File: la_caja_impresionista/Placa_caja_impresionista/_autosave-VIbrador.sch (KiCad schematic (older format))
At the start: 15 parts, among them U3 Buzzer, U4 HC-05, U5 Buzzer, U6 PiZeroW

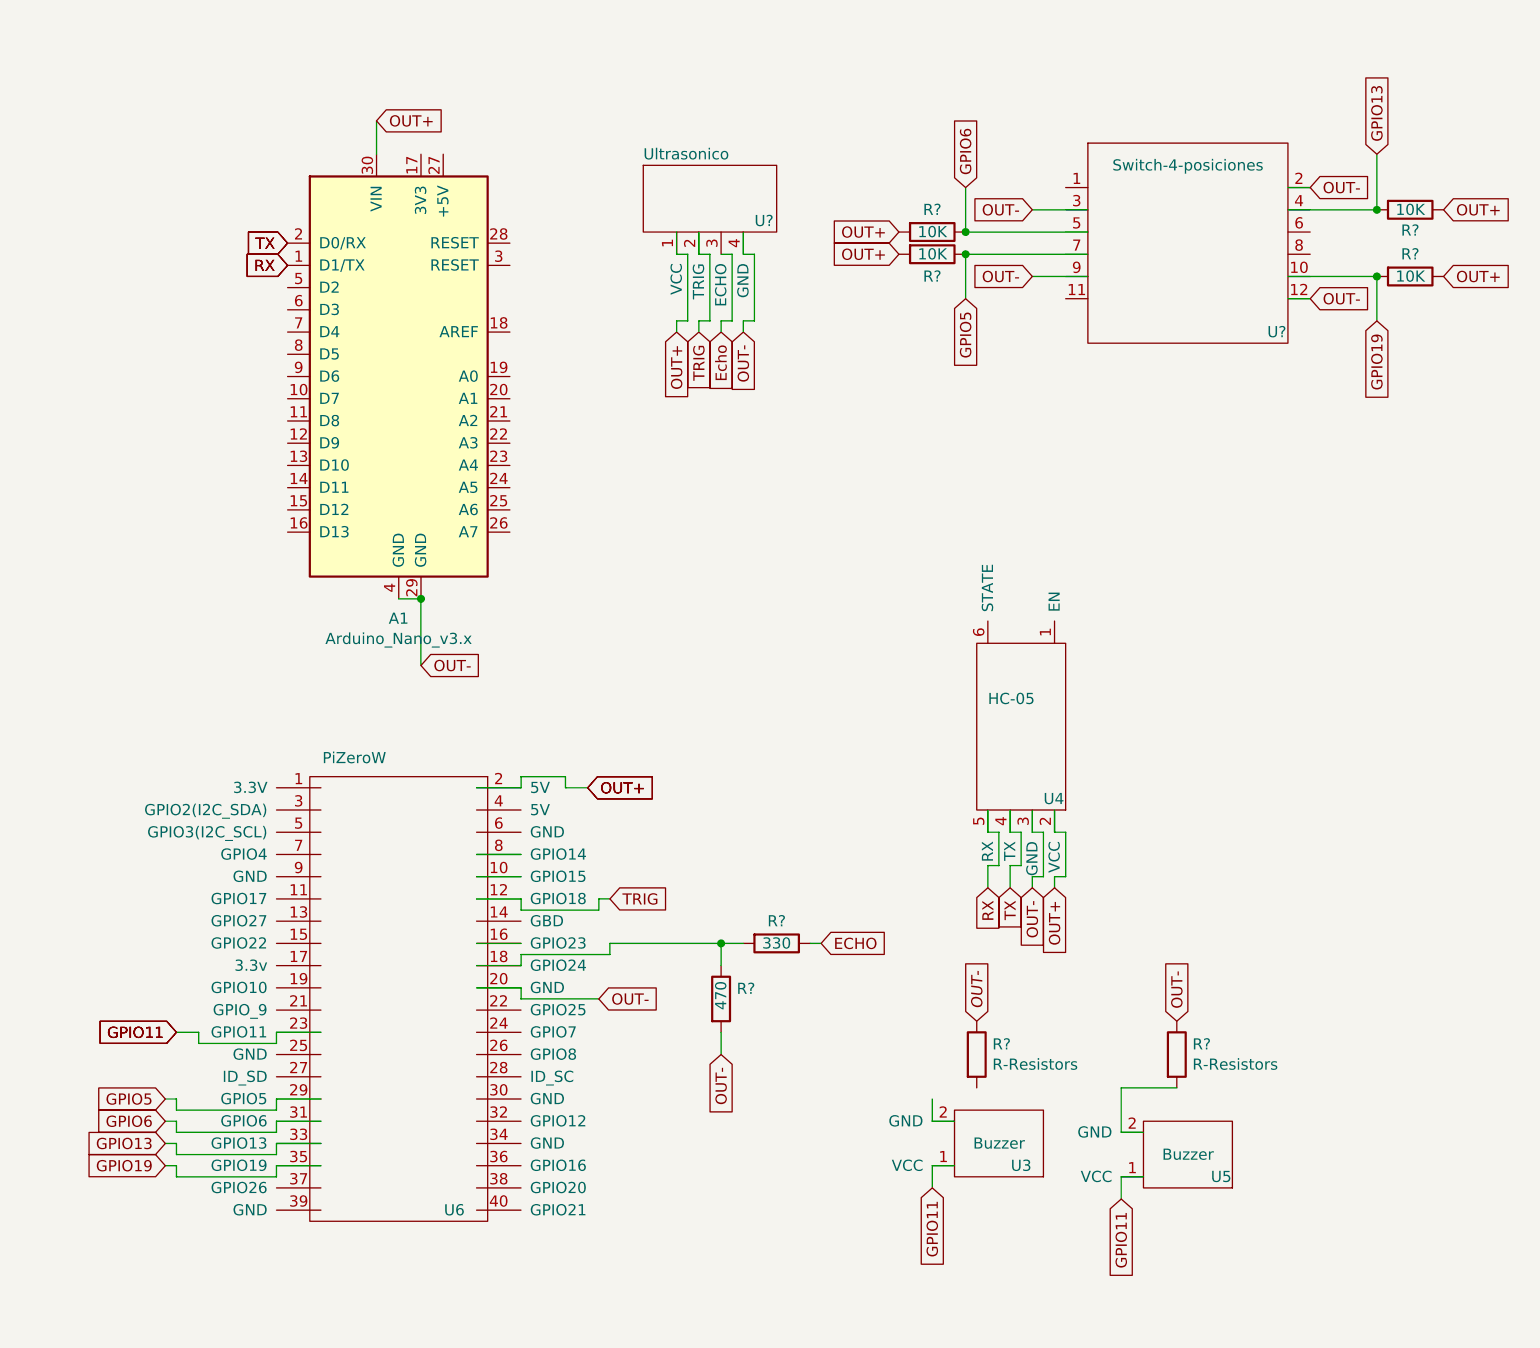
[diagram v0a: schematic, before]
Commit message: Conexiones PCB
Quedo conectado todo feo y como el orto pero esta conectado que es mejor que nada despues hay que revisar todas las conexiones y dejarlas facheras
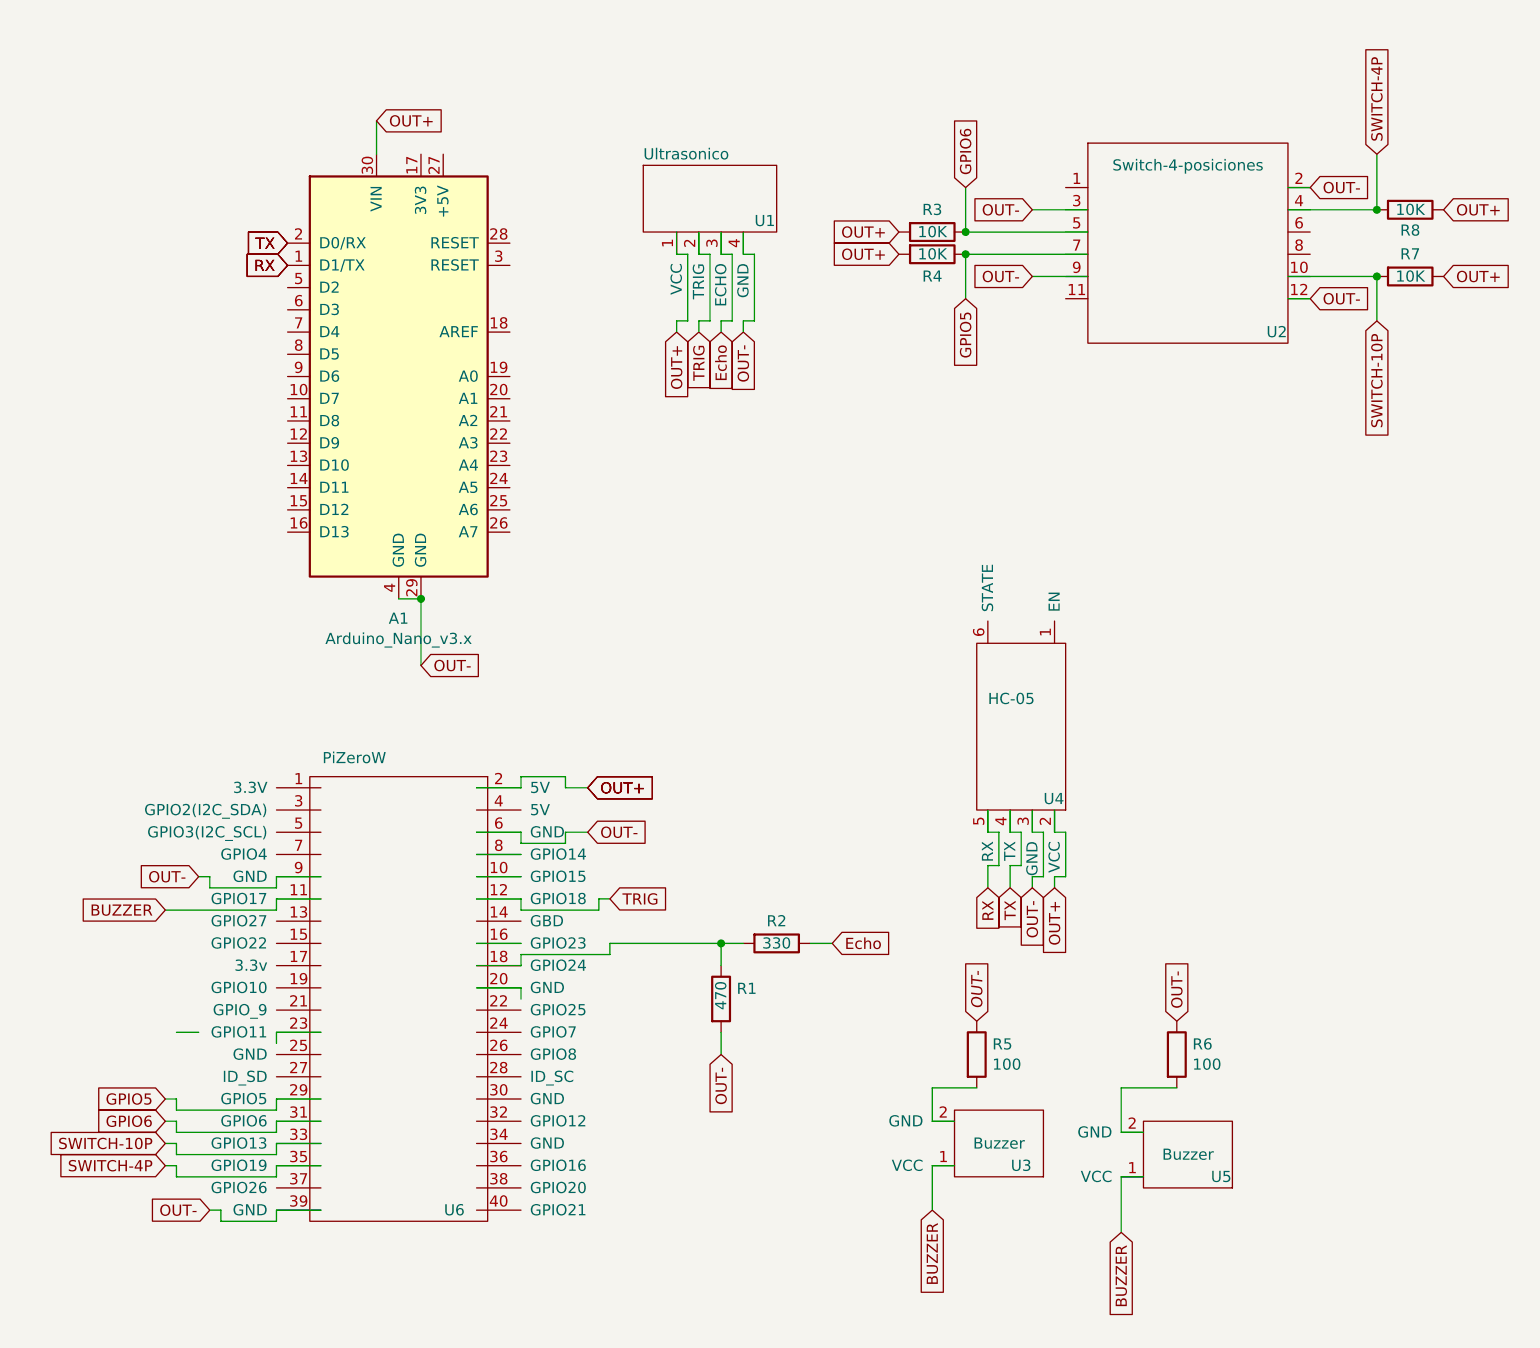
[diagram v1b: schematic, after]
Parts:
- A1: footprint Module:Arduino_Nano -> Raspberry:Arduino_Nano
- R1, R2, R3, R4, R7, R8: renamed from R?; footprint (none) -> devices:R_Axial_DIN0207_L6.3mm_D2.5mm_P10.16mm_Horizontal
- R5, R6: renamed from R?; value R-Resistors -> 100; footprint (none) -> devices:R_Axial_DIN0207_L6.3mm_D2.5mm_P10.16mm_Horizontal
- U1: renamed from U?; footprint (none) -> VibradorPCB:Ultrasonico
- U2: renamed from U?; footprint (none) -> VibradorPCB:Switch_4_posiciones
- U6: footprint Module:Raspberry_Pi_Zero_Socketed_THT_FaceDown_MountingHoles -> Raspberry:Raspberry_Pi_Zero_Socketed_THT_FaceDown_MountingHoles
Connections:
- net labels added: BUZZER, SWITCH-10P, SWITCH-4P
- net labels removed: ECHO, GPIO11, GPIO13, GPIO19
- wire segments 113 -> 130
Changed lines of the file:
@@
 Wire Wire Line
 	5350 6050 5250 6050
-Wire Wire Line
-	5250 6050 5250 6150
 Text GLabel 5450 5400 1    50   Input Italic 0
 OUT-
-Wire Wire Line
-	5250 5850 5250 5750
 Wire Wire Line
 	5250 5850 5350 5850
@@
 Wire Wire Line
 	6200 6100 6100 6100
-Wire Wire Line
-	6100 6100 6100 6200
 Text GLabel 6350 5400 1    50   Input ~ 0
 OUT-
@@
 $EndComp
 $Comp
-L VIbrador-rescue:PiZeroW U6
-U 1 1 5E9167F3
-P 2800 4300
-F 0 "U6" H 3100 2350 50  0000 C CNN
-F 1 "PiZeroW" H 2650 4384 50  0000 C CNN
-F 2 "Module:Raspberry_Pi_Zero_Socketed_THT_FaceDown_MountingHoles" H 2800 4300 50  0001 C CNN
-F 3 "" H 2800 4300 50  0001 C CNN
-	1    2800 4300
-	1    0    0    -1
-$EndComp
-$Comp
 L VIbrador-rescue:Arduino_Nano_v3.x-MCU_Module-VIbrador-rescue A1
 U 1 1 5E91EE2F
@@
 F 0 "A1" H 2850 1411 50  0000 C CNN
 F 1 "Arduino_Nano_v3.x" H 2850 1320 50  0000 C CNN
-F 2 "Module:Arduino_Nano" H 3000 1550 50  0001 L CNN
+F 2 "Raspberry:Arduino_Nano" H 3000 1550 50  0001 L CNN
 F 3 "http://www.mouser.com/pdfdocs/Gravitech_Arduino_Nano3_0.pdf" H 2850 1500 50  0001 C CNN
 	1    2850 2500
@@
 Wire Wire Line
 	3400 4350 3200 4350
-Text GLabel 3750 5300 2    50   Input ~ 0
+Text GLabel 3700 4550 2    50   Input ~ 0
 OUT-
 Wire Wire Line
@@
 Wire Wire Line
 	3400 5150 3200 5150
-Text GLabel 5250 6150 3    50   Input ~ 0
-GPIO11
-Text GLabel 6100 6200 3    50   Input ~ 0
-GPIO11
-Text GLabel 1850 5450 0    50   Input ~ 0
-GPIO11
 Wire Wire Line
 	2500 5450 2300 5450
 Wire Wire Line
 	2300 5450 2300 5500
-Wire Wire Line
-	2300 5500 1950 5500
-Wire Wire Line
-	1950 5500 1950 5450
 Wire Wire Line
 	1950 5450 1850 5450
@@
 RX
 $Comp
-L VIbrador-rescue:Ultrasonico-VIbrador-rescue U?
+L VIbrador-rescue:Ultrasonico-VIbrador-rescue U1
 U 1 1 5F11CF15
 P 4250 1600
-F 0 "U?" H 4450 1400 50  0000 L CNN
+F 0 "U1" H 4450 1400 50  0000 L CNN
 F 1 "Ultrasonico" H 3950 1700 50  0000 L CNN
-F 2 "" H 4250 1600 50  0001 C CNN
+F 2 "VibradorPCB:Ultrasonico" H 4250 1600 50  0001 C CNN
 F 3 "" H 4250 1600 50  0001 C CNN
 	1    4250 1600
@@
 Text GLabel 3700 4350 2    50   Input ~ 0
 OUT+
-Text GLabel 4750 5050 2    50   Input ~ 0
-ECHO
-Wire Wire Line
-	3400 5300 3750 5300
 Wire Wire Line
 	3400 5150 3400 5100
@@
 	3800 5100 3800 5050
 $Comp
-L VIbrador-rescue:R-Resistors R?
+L VIbrador-rescue:R-Resistors R1
 U 1 1 5F12F5BA
 P 4300 5300
-F 0 "R?" H 4370 5346 50  0000 L CNN
+F 0 "R1" H 4370 5346 50  0000 L CNN
 F 1 "470" V 4300 5250 50  0000 L CNN
-F 2 "" V 4230 5300 50  0001 C CNN
+F 2 "devices:R_Axial_DIN0207_L6.3mm_D2.5mm_P10.16mm_Horizontal" V 4230 5300 50  0001 C CNN
 F 3 "~" H 4300 5300 50  0001 C CNN
 	1    4300 5300
@@
 $EndComp
 $Comp
-L VIbrador-rescue:R-Resistors R?
+L VIbrador-rescue:R-Resistors R2
 U 1 1 5F12598C
 P 4550 5050
-F 0 "R?" V 4450 5050 50  0000 C CNN
+F 0 "R2" V 4450 5050 50  0000 C CNN
 F 1 "330" V 4550 5050 50  0000 C CNN
-F 2 "" V 4480 5050 50  0001 C CNN
+F 2 "devices:R_Axial_DIN0207_L6.3mm_D2.5mm_P10.16mm_Horizontal" V 4480 5050 50  0001 C CNN
 F 3 "~" H 4550 5050 50  0001 C CNN
 	1    4550 5050
@@
 $EndComp
 Wire Wire Line
-	4750 5050 4700 5050
-Wire Wire Line
 	3800 5050 4300 5050
 Wire Wire Line
@@
 	4300 5450 4300 5550
 $Comp
-L VIbrador-rescue:Switch-4-posiciones-VIbrador-rescue U?
+L VIbrador-rescue:Switch-4-posiciones-VIbrador-rescue U2
 U 1 1 5F14136B
 P 6450 1650
-F 0 "U?" H 6800 1000 50  0000 C CNN
+F 0 "U2" H 6800 1000 50  0000 C CNN
 F 1 "Switch-4-posiciones" H 6400 1750 50  0000 C CNN
-F 2 "" H 6450 1650 50  0001 C CNN
+F 2 "VibradorPCB:Switch_4_posiciones" H 6450 1650 50  0001 C CNN
 F 3 "" H 6450 1650 50  0001 C CNN
 	1    6450 1650
@@
 	5950 2050 5700 2050
 $Comp
-L VIbrador-rescue:R-Resistors R?
+L VIbrador-rescue:R-Resistors R7
 U 1 1 5F14B51D
 P 7400 1750
-F 0 "R?" V 7600 1750 50  0000 C CNN
+F 0 "R7" V 7600 1750 50  0000 C CNN
 F 1 "10K" V 7400 1750 50  0000 C CNN
-F 2 "" V 7330 1750 50  0001 C CNN
+F 2 "devices:R_Axial_DIN0207_L6.3mm_D2.5mm_P10.16mm_Horizontal" V 7330 1750 50  0001 C CNN
 F 3 "~" H 7400 1750 50  0001 C CNN
 	1    7400 1750
@@
 OUT+
 $Comp
-L VIbrador-rescue:R-Resistors R?
+L VIbrador-rescue:R-Resistors R3
 U 1 1 5F14E26A
 P 5250 1850
-F 0 "R?" V 5150 1850 50  0000 C CNN
+F 0 "R3" V 5150 1850 50  0000 C CNN
 F 1 "10K" V 5250 1850 50  0000 C CNN
-F 2 "" V 5180 1850 50  0001 C CNN
+F 2 "devices:R_Axial_DIN0207_L6.3mm_D2.5mm_P10.16mm_Horizontal" V 5180 1850 50  0001 C CNN
 F 3 "~" H 5250 1850 50  0001 C CNN
 	1    5250 1850
@@
 $EndComp
 $Comp
-L VIbrador-rescue:R-Resistors R?
+L VIbrador-rescue:R-Resistors R4
 U 1 1 5F14E782
 P 5250 1950
-F 0 "R?" V 5350 1950 50  0000 C CNN
+F 0 "R4" V 5350 1950 50  0000 C CNN
 F 1 "10K" V 5250 1950 50  0000 C CNN
-F 2 "" V 5180 1950 50  0001 C CNN
+F 2 "devices:R_Axial_DIN0207_L6.3mm_D2.5mm_P10.16mm_Horizontal" V 5180 1950 50  0001 C CNN
 F 3 "~" H 5250 1950 50  0001 C CNN
 	1    5250 1950
@@
 Text GLabel 7550 2050 2    50   Input ~ 0
 OUT+
-Text GLabel 1850 5450 0    50   Input ~ 0
-GPIO11
 Text GLabel 2350 1900 0    50   Input ~ 0
 TX
@@
 RX
 $Comp
-L VIbrador-rescue:R-Resistors R?
+L VIbrador-rescue:R-Resistors R8
 U 1 1 5F154336
 P 7400 2050
-F 0 "R?" V 7193 2050 50  0000 C CNN
+F 0 "R8" V 7193 2050 50  0000 C CNN
 F 1 "10K" V 7400 2050 50  0000 C CNN
-F 2 "" V 7330 2050 50  0001 C CNN
+F 2 "devices:R_Axial_DIN0207_L6.3mm_D2.5mm_P10.16mm_Horizontal" V 7330 2050 50  0001 C CNN
 F 3 "~" H 7400 2050 50  0001 C CNN
 	1    7400 2050
@@
 Text GLabel 5400 1650 1    50   Input ~ 0
 GPIO6
-Text GLabel 7250 1500 1    50   Input ~ 0
-GPIO13
 Text GLabel 7250 2250 3    50   Input ~ 0
-GPIO19
+SWITCH-10P
 Wire Wire Line
 	7250 1500 7250 1750
@@
 Text GLabel 1800 5850 0    50   Input ~ 0
 GPIO6
+Text GLabel 1800 6050 0    50   Input ~ 0
+SWITCH-4P
 Text GLabel 1800 5950 0    50   Input ~ 0
-GPIO13
-Text GLabel 1800 6050 0    50   Input ~ 0
-GPIO19
+SWITCH-10P
 Wire Wire Line
 	2500 5750 2300 5750
@@
 	2300 6050 2500 6050
 $Comp
-L VIbrador-rescue:R-Resistors R?
+L VIbrador-rescue:R-Resistors R6
 U 1 1 5F166DD1
 P 6350 5550
-F 0 "R?" H 6420 5596 50  0000 L CNN
-F 1 "R-Resistors" H 6420 5505 50  0000 L CNN
-F 2 "" V 6280 5550 50  0001 C CNN
+F 0 "R6" H 6420 5596 50  0000 L CNN
+F 1 "100" H 6420 5505 50  0000 L CNN
+F 2 "devices:R_Axial_DIN0207_L6.3mm_D2.5mm_P10.16mm_Horizontal" V 6280 5550 50  0001 C CNN
 F 3 "" H 6350 5550 50  0001 C CNN
 	1    6350 5550
@@
 $EndComp
 $Comp
-L VIbrador-rescue:R-Resistors R?
+L VIbrador-rescue:R-Resistors R5
 U 1 1 5F1677D6
 P 5450 5550
-F 0 "R?" H 5520 5596 50  0000 L CNN
-F 1 "R-Resistors" H 5520 5505 50  0000 L CNN
-F 2 "" V 5380 5550 50  0001 C CNN
+F 0 "R5" H 5520 5596 50  0000 L CNN
+F 1 "100" H 5520 5505 50  0000 L CNN
+F 2 "devices:R_Axial_DIN0207_L6.3mm_D2.5mm_P10.16mm_Horizontal" V 5380 5550 50  0001 C CNN
 F 3 "" H 5450 5550 50  0001 C CNN
 	1    5450 5550
@@
 Wire Wire Line
 	6100 5700 6100 5900
+Wire Wire Line
+	5250 5700 5250 5850
+Wire Wire Line
+	5450 5700 5250 5700
+Wire Wire Line
+	4300 1950 4300 1850
+Wire Wire Line
+	4700 5050 4800 5050
+Text GLabel 4800 5050 2    50   Input ~ 0
+Echo
+Wire Wire Line
+	3700 4550 3600 4550
+Wire Wire Line
+	3600 4550 3600 4600
+Wire Wire Line
+	3600 4600 3400 4600
+Wire Wire Line
+	3400 4600 3400 4550
+Wire Wire Line
+	3400 4550 3200 4550
+Text GLabel 1950 4750 0    50   Input ~ 0
+OUT-
+Wire Wire Line
+	2500 4750 2300 4750
+Wire Wire Line
+	2300 4750 2300 4800
+Wire Wire Line
+	2300 4800 2000 4800
+Wire Wire Line
+	2000 4800 2000 4750
+Wire Wire Line
+	2000 4750 1950 4750
+Text GLabel 2000 6250 0    50   Input ~ 0
+OUT-
+Wire Wire Line
+	2500 6250 2300 6250
+Wire Wire Line
+	2300 6250 2300 6300
+Wire Wire Line
+	2050 6300 2050 6250
+Wire Wire Line
+	2050 6250 2000 6250
+Wire Wire Line
+	2050 6300 2300 6300
+Text GLabel 5250 6250 3    50   Input ~ 0
+BUZZER
+Text GLabel 6100 6350 3    50   Input ~ 0
+BUZZER
+Wire Wire Line
+	6100 6100 6100 6350
+Wire Wire Line
+	5250 6050 5250 6250
+$Comp
+L VIbrador-rescue:PiZeroW U6
+U 1 1 5E9167F3
+P 2800 4300
+F 0 "U6" H 3100 2350 50  0000 C CNN
+F 1 "PiZeroW" H 2650 4384 50  0000 C CNN
+F 2 "Raspberry:Raspberry_Pi_Zero_Socketed_THT_FaceDown_MountingHoles" H 2800 4300 50  0001 C CNN
+F 3 "" H 2800 4300 50  0001 C CNN
+	1    2800 4300
+	1    0    0    -1
+$EndComp
+Text GLabel 1800 4900 0    50   Input ~ 0
+BUZZER
+Wire Wire Line
+	2500 4850 2300 4850
+Wire Wire Line
+	2300 4850 2300 4900
+Wire Wire Line
+	2300 4900 1800 4900
+Text GLabel 7250 1500 1    50   Input ~ 0
+SWITCH-4P
 $EndSCHEMATC

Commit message: PCB Terminado
Se actualizaron algunos pines de la raspberry ya que al principio se eligio al azar los que iban conectados a el switch y se fue viendo como convenia mas
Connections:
- net labels added: SWITCH-5P
- net labels removed: GPIO6
- wire segments 130 -> 144
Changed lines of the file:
@@
 Wire Wire Line
 	5350 6050 5250 6050
-Text GLabel 5450 5400 1    50   Input Italic 0
-OUT-
 Wire Wire Line
 	5250 5850 5350 5850
@@
 GPIO5
 Text GLabel 5400 1650 1    50   Input ~ 0
-GPIO6
+SWITCH-5P
 Text GLabel 7250 2250 3    50   Input ~ 0
 SWITCH-10P
@@
 Text GLabel 1800 5750 0    50   Input ~ 0
 GPIO5
-Text GLabel 1800 5850 0    50   Input ~ 0
-GPIO6
-Text GLabel 1800 6050 0    50   Input ~ 0
+Text GLabel 3800 6250 2    50   Input ~ 0
 SWITCH-4P
-Text GLabel 1800 5950 0    50   Input ~ 0
+Text GLabel 3800 4650 2    50   Input ~ 0
 SWITCH-10P
 Wire Wire Line
@@
 Text GLabel 7250 1500 1    50   Input ~ 0
 SWITCH-4P
+Text GLabel 5450 5400 1    50   Input ~ 0
+OUT-
+Wire Wire Line
+	3800 4650 3750 4650
+Wire Wire Line
+	3750 4650 3750 4700
+Wire Wire Line
+	3750 4700 3400 4700
+Wire Wire Line
+	3400 4700 3400 4650
+Text GLabel 3800 6150 2    50   Input ~ 0
+SWITCH-5P
+Wire Wire Line
+	3800 6150 3750 6150
+Wire Wire Line
+	3750 6150 3750 6200
+Wire Wire Line
+	3750 6200 3400 6200
+Wire Wire Line
+	3400 6200 3400 6150
+Wire Wire Line
+	3400 6150 3200 6150
+Wire Wire Line
+	3800 6250 3750 6250
+Wire Wire Line
+	3750 6250 3750 6300
+Wire Wire Line
+	3750 6300 3400 6300
+Wire Wire Line
+	3400 6300 3400 6250
+Wire Wire Line
+	3400 6250 3200 6250
 $EndSCHEMATC
